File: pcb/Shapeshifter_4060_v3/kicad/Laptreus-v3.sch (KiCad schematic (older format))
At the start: 96 parts

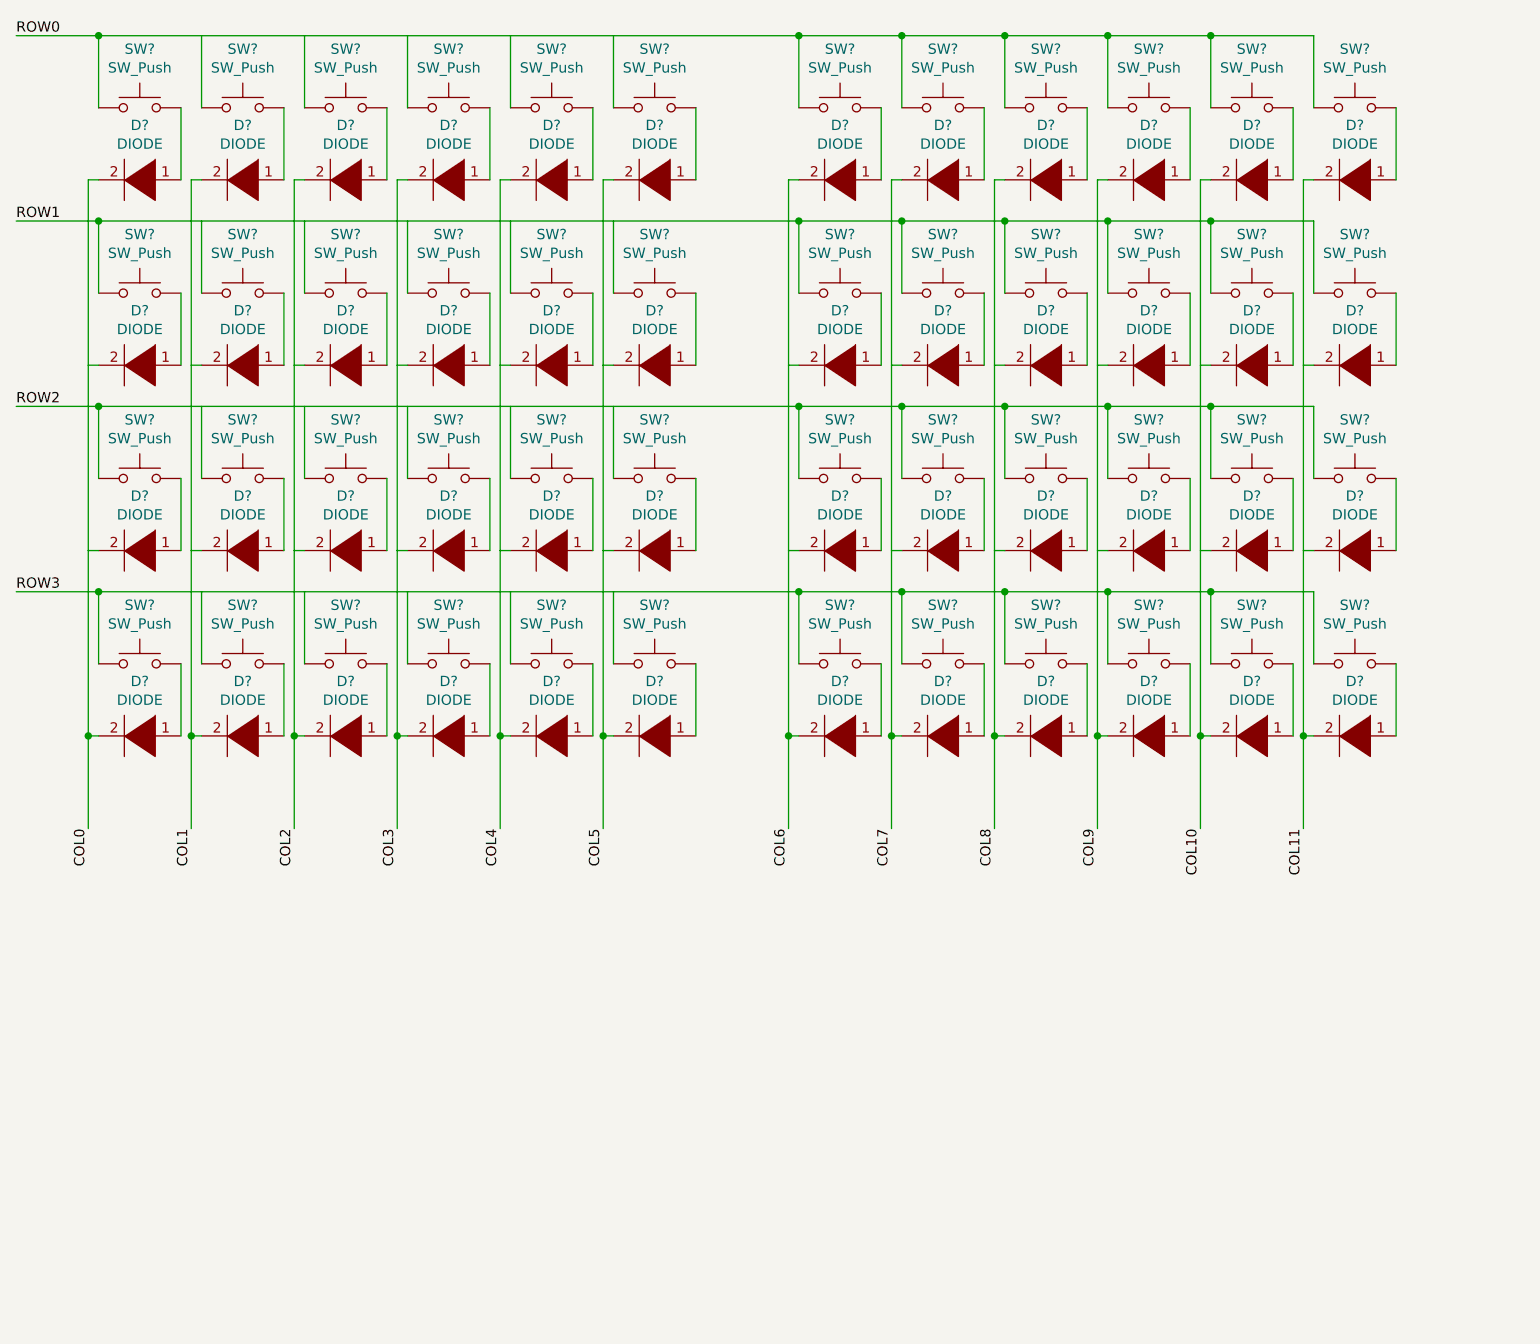
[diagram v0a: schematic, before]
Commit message: Update footprints for all objects on the PCB and annotate schema
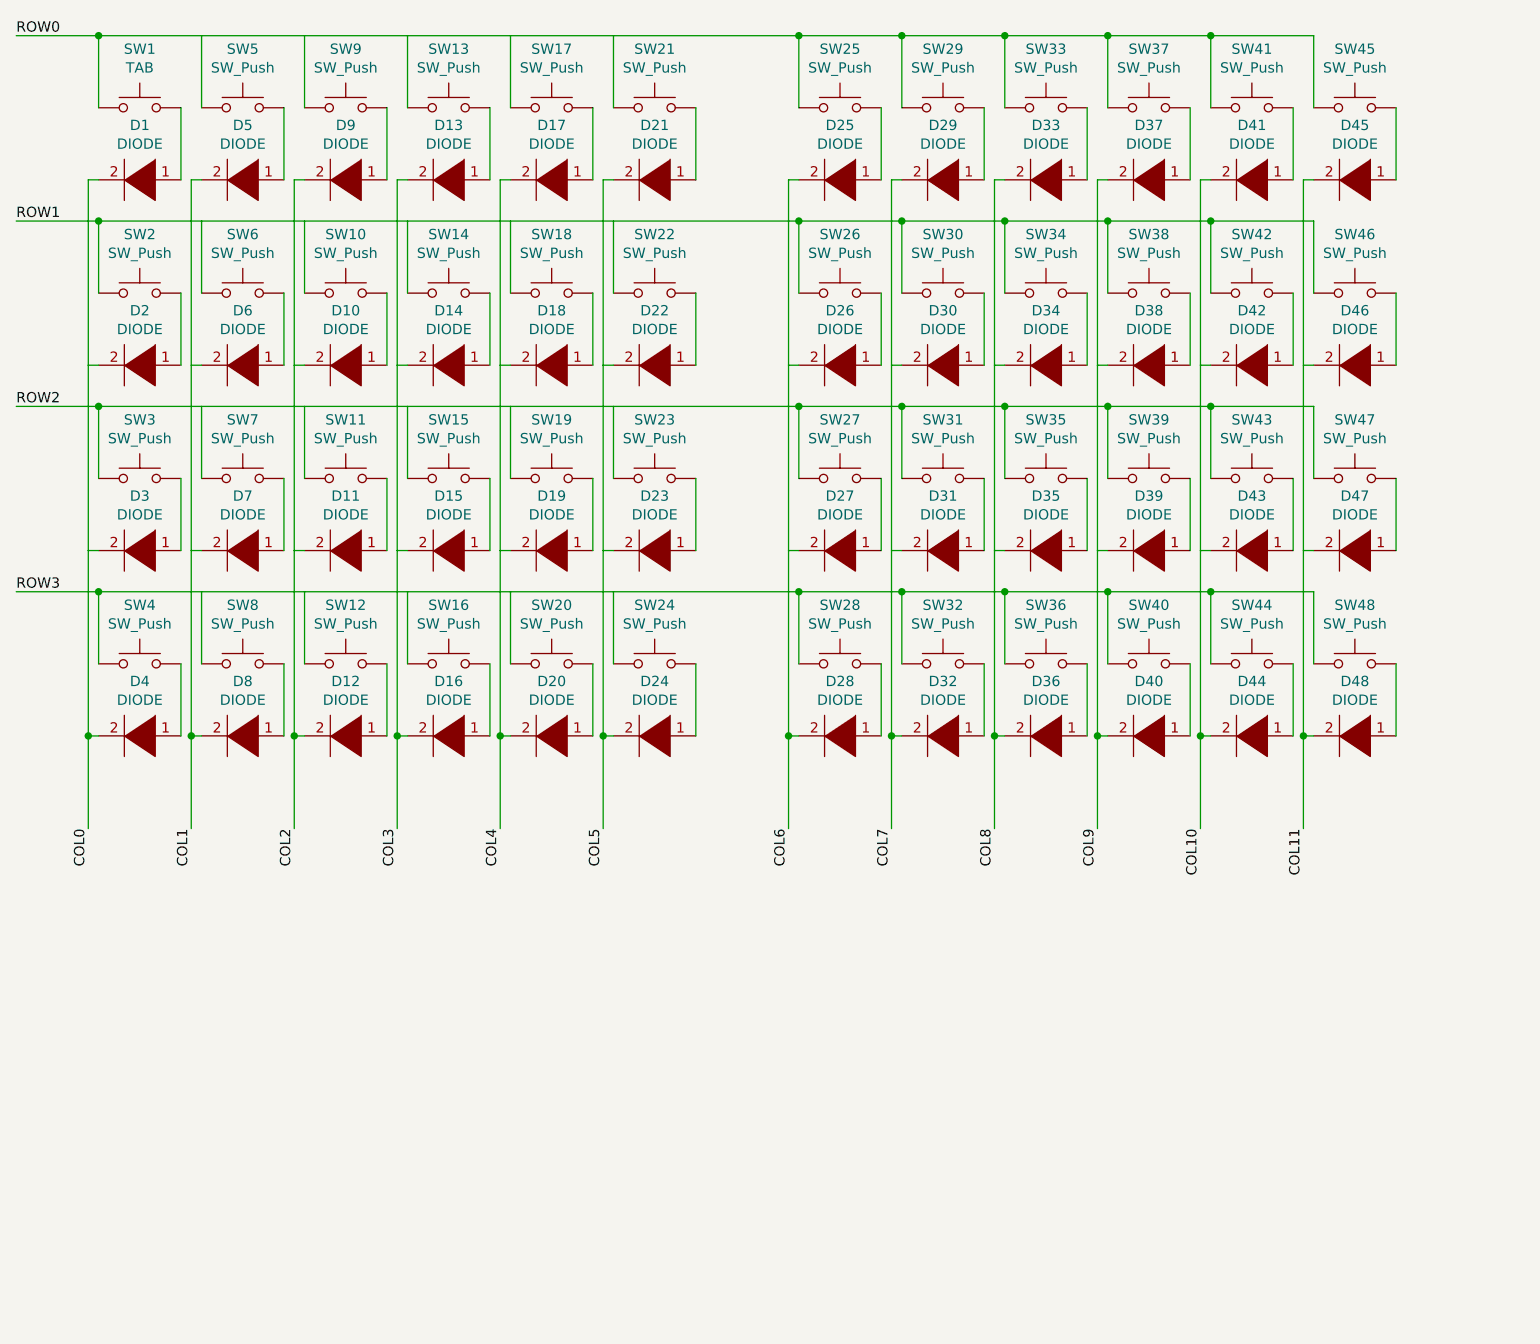
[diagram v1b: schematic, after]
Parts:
- SW1: renamed from SW?; value SW_Push -> TAB
- gave numbers to parts that had none: 95

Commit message: Update schema annotations to be correct and label each switch
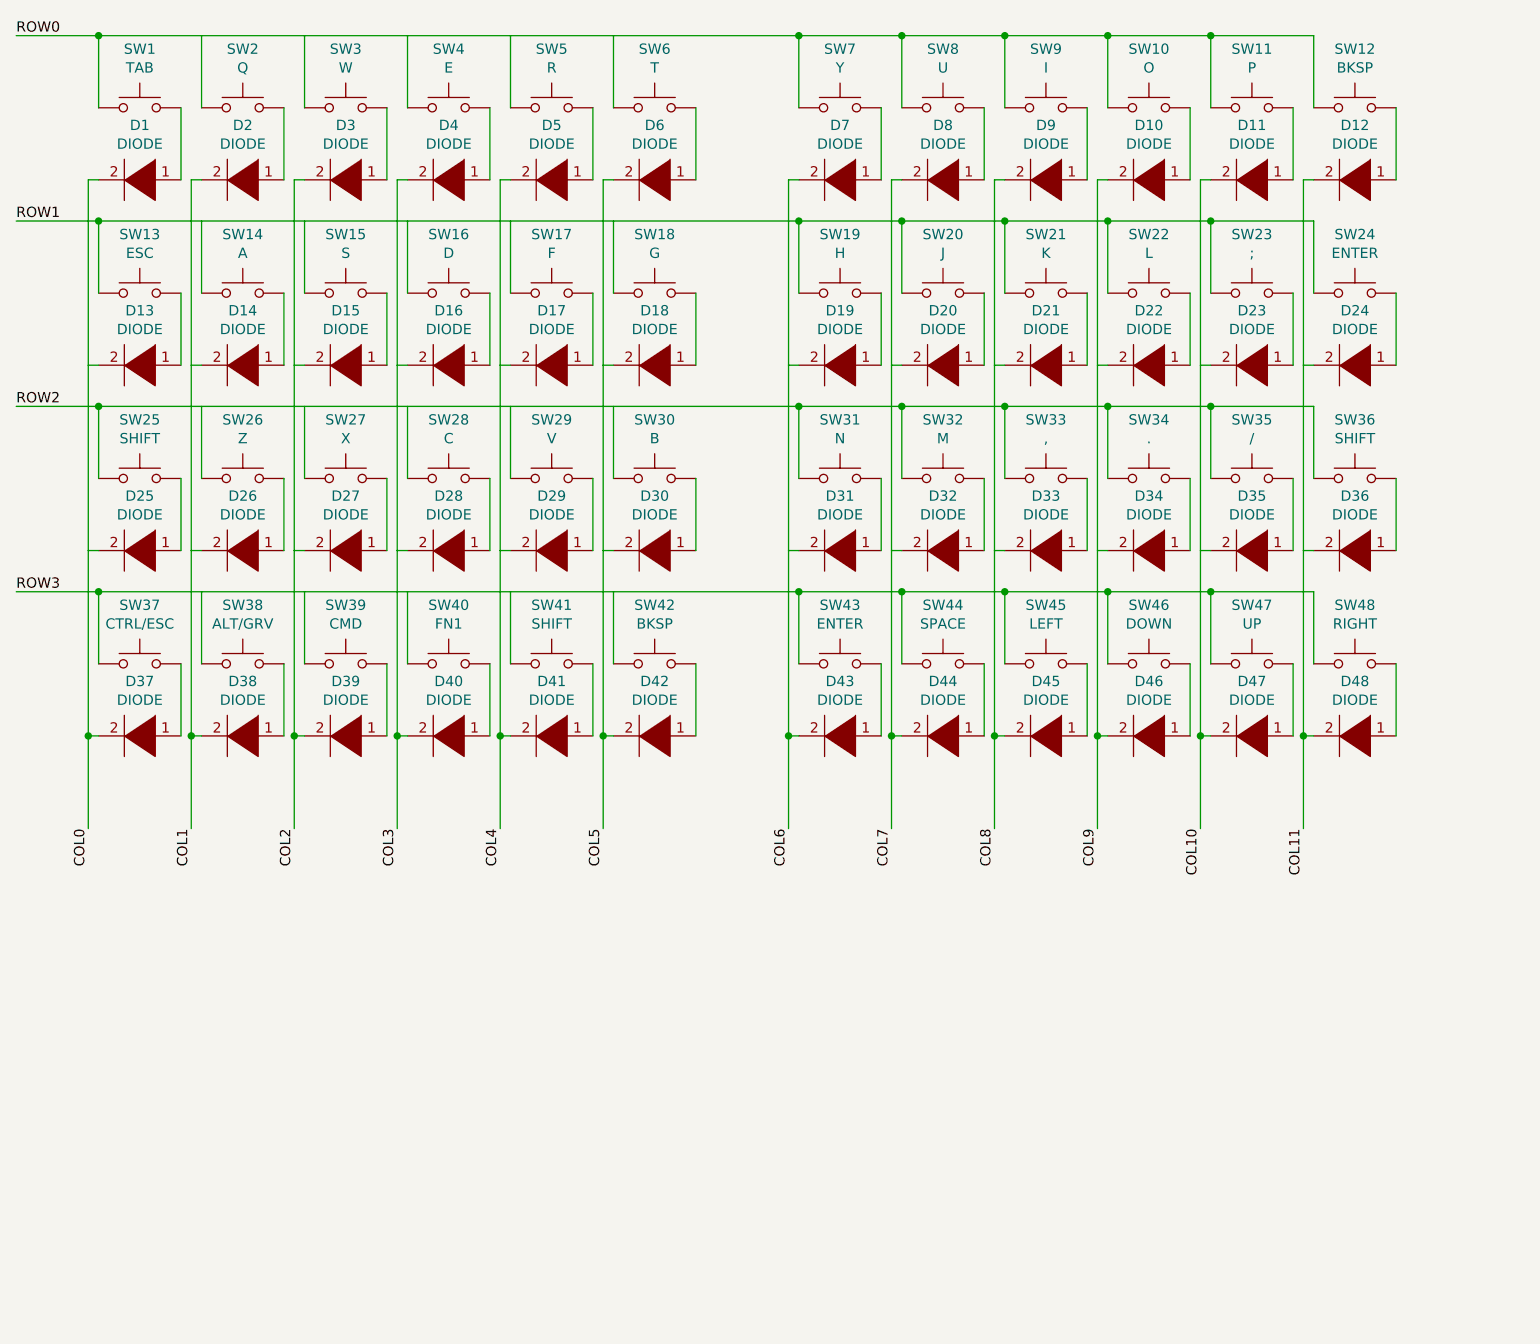
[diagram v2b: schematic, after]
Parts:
- D1: footprint (none) -> Kitsune-Footprints:Diode-dual
- D10: renamed from D37; footprint (none) -> Kitsune-Footprints:Diode-dual
- D11: renamed from D41; footprint (none) -> Kitsune-Footprints:Diode-dual
- D12: renamed from D45; footprint (none) -> Kitsune-Footprints:Diode-dual
- D13: renamed from D2; footprint (none) -> Kitsune-Footprints:Diode-dual
- D14: renamed from D6; footprint (none) -> Kitsune-Footprints:Diode-dual
- D15: renamed from D10; footprint (none) -> Kitsune-Footprints:Diode-dual
- D16: renamed from D14; footprint (none) -> Kitsune-Footprints:Diode-dual
- D17: renamed from D18; footprint (none) -> Kitsune-Footprints:Diode-dual
- D18: renamed from D22; footprint (none) -> Kitsune-Footprints:Diode-dual
- D19: renamed from D26; footprint (none) -> Kitsune-Footprints:Diode-dual
- D2: renamed from D5; footprint (none) -> Kitsune-Footprints:Diode-dual
- D20: renamed from D30; footprint (none) -> Kitsune-Footprints:Diode-dual
- D21: renamed from D34; footprint (none) -> Kitsune-Footprints:Diode-dual
- D22: renamed from D38; footprint (none) -> Kitsune-Footprints:Diode-dual
- D23: renamed from D42; footprint (none) -> Kitsune-Footprints:Diode-dual
- D24: renamed from D46; footprint (none) -> Kitsune-Footprints:Diode-dual
- D25: renamed from D3; footprint (none) -> Kitsune-Footprints:Diode-dual
- D26: renamed from D7; footprint (none) -> Kitsune-Footprints:Diode-dual
- D27: renamed from D11; footprint (none) -> Kitsune-Footprints:Diode-dual
- D28: renamed from D15; footprint (none) -> Kitsune-Footprints:Diode-dual
- D29: renamed from D19; footprint (none) -> Kitsune-Footprints:Diode-dual
- D3: renamed from D9; footprint (none) -> Kitsune-Footprints:Diode-dual
- D30: renamed from D23; footprint (none) -> Kitsune-Footprints:Diode-dual
- D31: renamed from D27; footprint (none) -> Kitsune-Footprints:Diode-dual
- D32: renamed from D31; footprint (none) -> Kitsune-Footprints:Diode-dual
- D33: renamed from D35; footprint (none) -> Kitsune-Footprints:Diode-dual
- D34: renamed from D39; footprint (none) -> Kitsune-Footprints:Diode-dual
- D35: renamed from D43; footprint (none) -> Kitsune-Footprints:Diode-dual
- D36: renamed from D47; footprint (none) -> Kitsune-Footprints:Diode-dual
- D37: renamed from D4; footprint (none) -> Kitsune-Footprints:Diode-dual
- D38: renamed from D8; footprint (none) -> Kitsune-Footprints:Diode-dual
- D39: renamed from D12; footprint (none) -> Kitsune-Footprints:Diode-dual
- D4: renamed from D13; footprint (none) -> Kitsune-Footprints:Diode-dual
- D40: renamed from D16; footprint (none) -> Kitsune-Footprints:Diode-dual
- D41: renamed from D20; footprint (none) -> Kitsune-Footprints:Diode-dual
- D42: renamed from D24; footprint (none) -> Kitsune-Footprints:Diode-dual
- D43: renamed from D28; footprint (none) -> Kitsune-Footprints:Diode-dual
- D44: renamed from D32; footprint (none) -> Kitsune-Footprints:Diode-dual
- D45: renamed from D36; footprint (none) -> Kitsune-Footprints:Diode-dual
- D46: renamed from D40; footprint (none) -> Kitsune-Footprints:Diode-dual
- D47: renamed from D44; footprint (none) -> Kitsune-Footprints:Diode-dual
- D48, SW1: footprint (none) -> Kitsune-Footprints:Hybrid_Kailh_MX_Choc_Socket_Through_Hole_With_Diode
- D5: renamed from D17; footprint (none) -> Kitsune-Footprints:Diode-dual
- D6: renamed from D21; footprint (none) -> Kitsune-Footprints:Diode-dual
- D7: renamed from D25; footprint (none) -> Kitsune-Footprints:Diode-dual
- D8: renamed from D29; footprint (none) -> Kitsune-Footprints:Diode-dual
- D9: renamed from D33; footprint (none) -> Kitsune-Footprints:Diode-dual
- SW10: renamed from SW37; value SW_Push -> O; footprint (none) -> Kitsune-Footprints:Hybrid_Kailh_MX_Choc_Socket_Through_Hole_With_Diode
- SW11: renamed from SW41; value SW_Push -> P; footprint (none) -> Kitsune-Footprints:Hybrid_Kailh_MX_Choc_Socket_Through_Hole_With_Diode
- SW12: renamed from SW45; value SW_Push -> BKSP; footprint (none) -> Kitsune-Footprints:Hybrid_Kailh_MX_Choc_Socket_Through_Hole_With_Diode
- SW13: renamed from SW2; value SW_Push -> ESC; footprint (none) -> Kitsune-Footprints:Hybrid_Kailh_MX_Choc_Socket_Through_Hole_With_Diode
- SW14: renamed from SW6; value SW_Push -> A; footprint (none) -> Kitsune-Footprints:Hybrid_Kailh_MX_Choc_Socket_Through_Hole_With_Diode
- SW15: renamed from SW10; value SW_Push -> S; footprint (none) -> Kitsune-Footprints:Hybrid_Kailh_MX_Choc_Socket_Through_Hole_With_Diode
- SW16: renamed from SW14; value SW_Push -> D; footprint (none) -> Kitsune-Footprints:Hybrid_Kailh_MX_Choc_Socket_Through_Hole_With_Diode
- SW17: renamed from SW18; value SW_Push -> F; footprint (none) -> Kitsune-Footprints:Hybrid_Kailh_MX_Choc_Socket_Through_Hole_With_Diode
- SW18: renamed from SW22; value SW_Push -> G; footprint (none) -> Kitsune-Footprints:Hybrid_Kailh_MX_Choc_Socket_Through_Hole_With_Diode
- SW19: renamed from SW26; value SW_Push -> H; footprint (none) -> Kitsune-Footprints:Hybrid_Kailh_MX_Choc_Socket_Through_Hole_With_Diode
- SW2: renamed from SW5; value SW_Push -> Q; footprint (none) -> Kitsune-Footprints:Hybrid_Kailh_MX_Choc_Socket_Through_Hole_With_Diode
- SW20: renamed from SW30; value SW_Push -> J; footprint (none) -> Kitsune-Footprints:Hybrid_Kailh_MX_Choc_Socket_Through_Hole_With_Diode
- SW21: renamed from SW34; value SW_Push -> K; footprint (none) -> Kitsune-Footprints:Hybrid_Kailh_MX_Choc_Socket_Through_Hole_With_Diode
- SW22: renamed from SW38; value SW_Push -> L; footprint (none) -> Kitsune-Footprints:Hybrid_Kailh_MX_Choc_Socket_Through_Hole_With_Diode
- SW23: renamed from SW42; value SW_Push -> ;; footprint (none) -> Kitsune-Footprints:Hybrid_Kailh_MX_Choc_Socket_Through_Hole_With_Diode
- SW24: renamed from SW46; value SW_Push -> ENTER; footprint (none) -> Kitsune-Footprints:Hybrid_Kailh_MX_Choc_Socket_Through_Hole_With_Diode
- SW25: renamed from SW3; value SW_Push -> SHIFT; footprint (none) -> Kitsune-Footprints:Hybrid_Kailh_MX_Choc_Socket_Through_Hole_With_Diode
- SW26: renamed from SW7; value SW_Push -> Z; footprint (none) -> Kitsune-Footprints:Hybrid_Kailh_MX_Choc_Socket_Through_Hole_With_Diode
- SW27: renamed from SW11; value SW_Push -> X; footprint (none) -> Kitsune-Footprints:Hybrid_Kailh_MX_Choc_Socket_Through_Hole_With_Diode
- SW28: renamed from SW15; value SW_Push -> C; footprint (none) -> Kitsune-Footprints:Hybrid_Kailh_MX_Choc_Socket_Through_Hole_With_Diode
- SW29: renamed from SW19; value SW_Push -> V; footprint (none) -> Kitsune-Footprints:Hybrid_Kailh_MX_Choc_Socket_Through_Hole_With_Diode
- SW3: renamed from SW9; value SW_Push -> W; footprint (none) -> Kitsune-Footprints:Hybrid_Kailh_MX_Choc_Socket_Through_Hole_With_Diode
- SW30: renamed from SW23; value SW_Push -> B; footprint (none) -> Kitsune-Footprints:Hybrid_Kailh_MX_Choc_Socket_Through_Hole_With_Diode
- SW31: renamed from SW27; value SW_Push -> N; footprint (none) -> Kitsune-Footprints:Hybrid_Kailh_MX_Choc_Socket_Through_Hole_With_Diode
- SW32: renamed from SW31; value SW_Push -> M; footprint (none) -> Kitsune-Footprints:Hybrid_Kailh_MX_Choc_Socket_Through_Hole_With_Diode
- SW33: renamed from SW35; value SW_Push -> ,; footprint (none) -> Kitsune-Footprints:Hybrid_Kailh_MX_Choc_Socket_Through_Hole_With_Diode
- SW34: renamed from SW39; value SW_Push -> .; footprint (none) -> Kitsune-Footprints:Hybrid_Kailh_MX_Choc_Socket_Through_Hole_With_Diode
- SW35: renamed from SW43; value SW_Push -> /; footprint (none) -> Kitsune-Footprints:Hybrid_Kailh_MX_Choc_Socket_Through_Hole_With_Diode
- SW36: renamed from SW47; value SW_Push -> SHIFT; footprint (none) -> Kitsune-Footprints:Hybrid_Kailh_MX_Choc_Socket_Through_Hole_With_Diode
- SW37: renamed from SW4; value SW_Push -> CTRL/ESC; footprint (none) -> Kitsune-Footprints:Hybrid_Kailh_MX_Choc_Socket_Through_Hole_With_Diode
- SW38: renamed from SW8; value SW_Push -> ALT/GRV; footprint (none) -> Kitsune-Footprints:Hybrid_Kailh_MX_Choc_Socket_Through_Hole_With_Diode
- SW39: renamed from SW12; value SW_Push -> CMD; footprint (none) -> Kitsune-Footprints:Hybrid_Kailh_MX_Choc_Socket_Through_Hole_With_Diode
- SW4: renamed from SW13; value SW_Push -> E; footprint (none) -> Kitsune-Footprints:Hybrid_Kailh_MX_Choc_Socket_Through_Hole_With_Diode
- SW40: renamed from SW16; value SW_Push -> FN1; footprint (none) -> Kitsune-Footprints:Hybrid_Kailh_MX_Choc_Socket_Through_Hole_With_Diode
- SW41: renamed from SW20; value SW_Push -> SHIFT; footprint (none) -> Kitsune-Footprints:Hybrid_Kailh_MX_Choc_Socket_Through_Hole_With_Diode
- SW42: renamed from SW24; value SW_Push -> BKSP; footprint (none) -> Kitsune-Footprints:Hybrid_Kailh_MX_Choc_Socket_Through_Hole_With_Diode
- SW43: renamed from SW28; value SW_Push -> ENTER; footprint (none) -> Kitsune-Footprints:Hybrid_Kailh_MX_Choc_Socket_Through_Hole_With_Diode
- SW44: renamed from SW32; value SW_Push -> SPACE; footprint (none) -> Kitsune-Footprints:Hybrid_Kailh_MX_Choc_Socket_Through_Hole_With_Diode
- SW45: renamed from SW36; value SW_Push -> LEFT; footprint (none) -> Kitsune-Footprints:Hybrid_Kailh_MX_Choc_Socket_Through_Hole_With_Diode
- SW46: renamed from SW40; value SW_Push -> DOWN; footprint (none) -> Kitsune-Footprints:Hybrid_Kailh_MX_Choc_Socket_Through_Hole_With_Diode
- SW47: renamed from SW44; value SW_Push -> UP; footprint (none) -> Kitsune-Footprints:Hybrid_Kailh_MX_Choc_Socket_Through_Hole_With_Diode
- SW48: value SW_Push -> RIGHT; footprint (none) -> Kitsune-Footprints:Hybrid_Kailh_MX_Choc_Socket_Through_Hole_With_Diode
- SW5: renamed from SW17; value SW_Push -> R; footprint (none) -> Kitsune-Footprints:Hybrid_Kailh_MX_Choc_Socket_Through_Hole_With_Diode
- SW6: renamed from SW21; value SW_Push -> T; footprint (none) -> Kitsune-Footprints:Hybrid_Kailh_MX_Choc_Socket_Through_Hole_With_Diode
- SW7: renamed from SW25; value SW_Push -> Y; footprint (none) -> Kitsune-Footprints:Hybrid_Kailh_MX_Choc_Socket_Through_Hole_With_Diode
- SW8: renamed from SW29; value SW_Push -> U; footprint (none) -> Kitsune-Footprints:Hybrid_Kailh_MX_Choc_Socket_Through_Hole_With_Diode
- SW9: renamed from SW33; value SW_Push -> I; footprint (none) -> Kitsune-Footprints:Hybrid_Kailh_MX_Choc_Socket_Through_Hole_With_Diode

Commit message: Update diode positions on the pcb
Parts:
- D48: footprint Kitsune-Footprints:Hybrid_Kailh_MX_Choc_Socket_Through_Hole_With_Diode -> Kitsune-Footprints:Diode-dual
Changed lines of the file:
@@
 F 0 "D48" H 7400 4565 50  0000 C CNN
 F 1 "DIODE" H 7400 4474 50  0000 C CNN
-F 2 "Kitsune-Footprints:Hybrid_Kailh_MX_Choc_Socket_Through_Hole_With_Diode" H 7400 4300 50  0001 C CNN
+F 2 "Kitsune-Footprints:Diode-dual" H 7400 4300 50  0001 C CNN
 F 3 "~" H 7400 4300 50  0001 C CNN
 	1    7400 4300
